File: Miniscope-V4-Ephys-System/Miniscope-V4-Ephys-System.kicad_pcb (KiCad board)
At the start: 4 copper layers, 24.2 x 15.5 mm, 67 parts, among them J1 34 Circuit Slimslack Connector, J10 Conn_01x01, J11 Conn_01x01, J12 Conn_01x01, J13 Conn_01x01, J14 Conn_01x05, J15 Conn_01x01, J16 Conn_01x01, J17 Conn_01x01, J18 Conn_01x01, J19 Conn_01x01, J2 Conn_01x01, J20 Conn_01x01, J21 Conn_01x01, J22 Conn_01x01, J23 Conn_01x01, J24 Conn_01x01, J25 Conn_01x01, J26 Conn_01x01, J27 Conn_01x01, J28 Conn_01x01, J3 Conn_01x01, J4 Conn_01x01, J5 Conn_01x01, J6 Conn_01x01, J7 Conn_01x01, J8 Conn_01x01, J9 Conn_01x01, Q1 MMBT3904LP-7B, U1 RHD2132, U2 TXB0304RUT, U3 MCP1711T-30I/5X, U4 ATSAME70N21A-CN, U5 MCP1711T-18I/5X, Y1 SMD_CRYSTAL

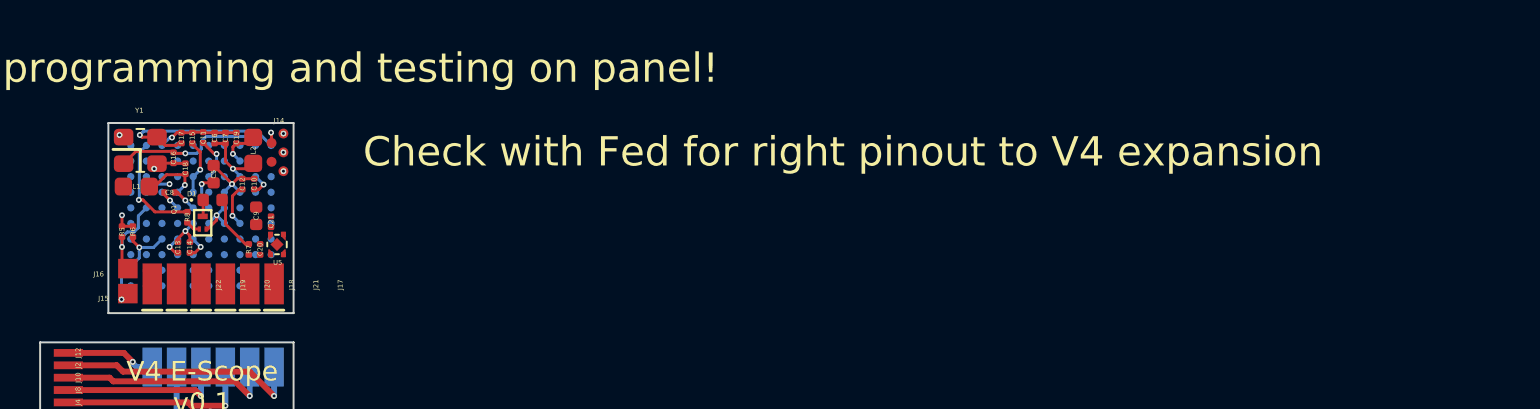
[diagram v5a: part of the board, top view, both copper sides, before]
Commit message: Finish routing of all PCBs. Need to double check before fabrication.
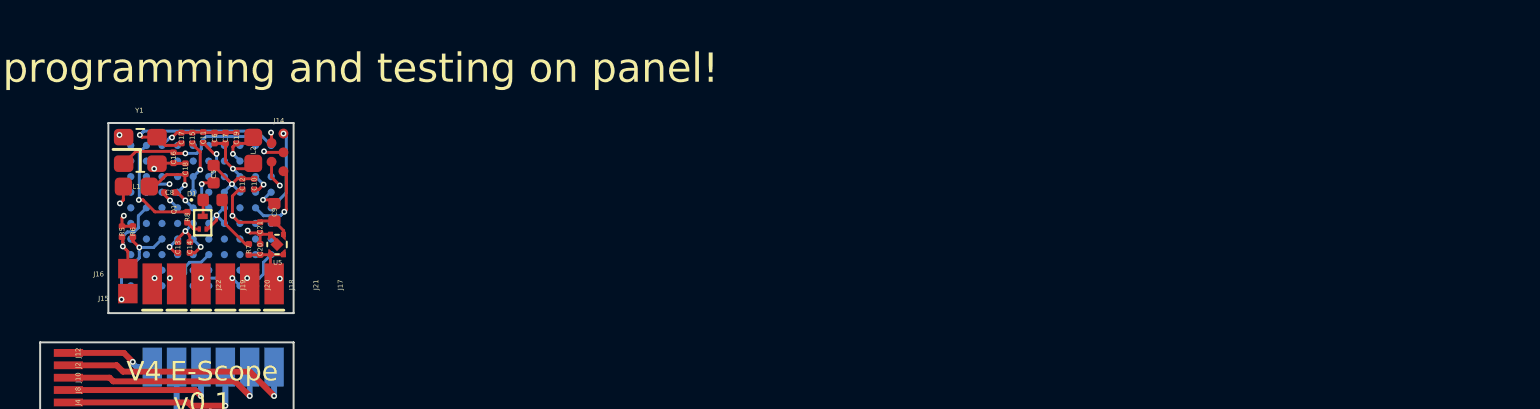
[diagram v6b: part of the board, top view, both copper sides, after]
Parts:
- moved C9 0.95 mm to (130.0, 124.1)
- moved C21 0.64 mm to (129.3, 124.9), turned to 270 degrees
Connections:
- J14 pad 1: +5V -> /MCU/TF
- J14 pad 2: /MCU/TF -> /MCU/TD
- J14 pad 3: /MCU/TD -> GND
- J14 pad 4: /MCU/TK -> +5V
- J14 pad 5: GND -> /MCU/TK
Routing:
- net /MCU/VDDCORE: track 7.81 -> 22.9 mm, vias 3 -> 4
- net +5V: track 20.7 -> 30.3 mm, vias 4 -> 5
- net /MCU/TD: track 1.36 -> 8.21 mm
- net GND: track 39.9 -> 44.6 mm, vias 16 -> 19
- net /MCU/TK: track 0.00 -> 3.91 mm, vias 0 -> 1
- net /MCU/TF: track 0.54 -> 4.19 mm
- net +1V8: track 11.2 -> 14.4 mm
- net /MCU/SPI0_MOSI: track 0.00 -> 2.70 mm, vias 0 -> 1
- net /MCU/SPI0_NPCS0: track 0.00 -> 2.08 mm, vias 0 -> 1
- net /MCU/SPI0_SPCK: track 0.00 -> 1.36 mm, vias 0 -> 1
- net /MCU/SPI0_MISO: track 0.00 -> 0.56 mm, vias 0 -> 1
- added copper zone on In2.Cu, net +1V8
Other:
- board text removed: "Check with Fed for right pinout to V4 expansion"

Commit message: Add files via upload
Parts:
- moved C10 3.98 mm to (129.0, 118.7)
- moved C12 3.98 mm to (128.4, 118.7)
- moved C13 3.98 mm to (125.1, 121.9)
- moved C14 3.98 mm to (125.7, 121.9)
- moved C15 3.98 mm to (125.8, 116.3)
- moved C17 3.98 mm to (125.2, 116.3)
- moved C18 3.98 mm to (125.5, 117.9)
- moved C19 3.98 mm to (128.1, 116.3)
- moved C6 3.98 mm to (126.9, 116.3)
- moved C7 3.98 mm to (127.5, 116.3)
- moved C8 3.98 mm to (124.6, 119.1)
- moved C9 3.98 mm to (130.0, 120.1)
- moved D1 3.98 mm to (126.8, 119.5)
- moved J14 3.98 mm to (130.5, 116.1)
- moved L1 3.98 mm to (122.9, 118.8)
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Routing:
- net (no net): vias 0 -> 4
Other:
- board size 24.2 x 15.5 mm -> 36.1 x 27.2 mm

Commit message: Revert "pcb file updated"
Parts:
- moved C10 3.98 mm to (129.0, 122.6)
- moved C12 3.98 mm to (128.4, 122.6)
- moved C13 3.98 mm to (125.1, 125.9)
- moved C14 3.98 mm to (125.7, 125.9)
- moved C15 3.98 mm to (125.8, 120.3)
- moved C17 3.98 mm to (125.2, 120.3)
- moved C18 3.98 mm to (125.5, 121.8)
- moved C19 3.98 mm to (128.1, 120.3)
- moved C6 3.98 mm to (126.9, 120.3)
- moved C7 3.98 mm to (127.5, 120.3)
- moved C8 3.98 mm to (124.6, 123.1)
- moved C9 3.98 mm to (130.0, 124.1)
- moved D1 3.98 mm to (126.8, 123.4)
- moved J14 3.98 mm to (130.5, 120.0)
- moved L1 3.98 mm to (122.9, 122.8)
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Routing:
- net (no net): vias 4 -> 0
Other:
- board size 36.1 x 27.2 mm -> 24.2 x 15.5 mm
